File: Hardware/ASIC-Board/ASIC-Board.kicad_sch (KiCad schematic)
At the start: 30 parts, among them J201 Conn_02x20_Odd_Even, J202 Keyboard, J203 Edge_Connector, U201 MegaDuck_Interface_CPU, U202 74LS241, U203 by ManCloud, Y201 Crystal

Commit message: fixed orientation of EXT-Header
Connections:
- net CP: now also J201.30 (Pin_30); no longer J201.12 (Pin_12)
- net CPG: now also J201.31 (Pin_31); no longer J201.9 (Pin_9)
- net CPL: now also J201.27 (Pin_27); no longer J201.13 (Pin_13)
- net EDGE_14: now also J201.25 (Pin_25); no longer J201.15 (Pin_15)
- net FR: now also J201.34 (Pin_34); no longer J201.8 (Pin_8)
- net GND: now also J201.26 (Pin_26); no longer J201.16 (Pin_16)
- net LD0: now also J201.32 (Pin_32); no longer J201.10 (Pin_10)
- net LD1: now also J201.33 (Pin_33); no longer J201.7 (Pin_7)
- net P14_EXT: now also J201.35 (Pin_35); no longer J201.5 (Pin_5)
- net S: now also J201.28 (Pin_28); no longer J201.14 (Pin_14)
- net SCK_EXT: now also J201.36 (Pin_36); no longer J201.6 (Pin_6)
- net SIN_EXT: now also J201.37 (Pin_37); no longer J201.3 (Pin_3)
- net SOUT_EXT: now also J201.38 (Pin_38); no longer J201.4 (Pin_4)
- net ST: now also J201.29 (Pin_29); no longer J201.11 (Pin_11)
- net VCC: now also J201.39 (Pin_39), J201.40 (Pin_40); no longer J201.1 (Pin_1), J201.2 (Pin_2)
- net at R206.2, U202.2 (I0a): now also J201.20 (Pin_20); no longer J201.22 (Pin_22)
- net at R203.2, U202.11 (I0b): now also J201.22 (Pin_22); no longer J201.20 (Pin_20)
- net at R201.2, U202.13 (I1b): now also J201.21 (Pin_21); no longer J201.19 (Pin_19)
- net at R205.2, U202.4 (I1a): now also J201.15 (Pin_15); no longer J201.25 (Pin_25)
- net at J201.17 (Pin_17): now also U201.68; no longer U201.70
- net at J201.18 (Pin_18): now also U201.69; no longer U201.71
- net at U201.6: now also J201.19 (Pin_19); no longer J201.21 (Pin_21)
- net at J201.23 (Pin_23): now also U201.70; no longer U201.68
- net at J201.24 (Pin_24): now also U201.71; no longer U201.69
- net at U202.17 (I3b): now also J201.16 (Pin_16); no longer J201.26 (Pin_26)
- net at U201.65: now also J201.13 (Pin_13); no longer J201.27 (Pin_27)
- net at U202.15 (I2b): now also J201.14 (Pin_14); no longer J201.28 (Pin_28)
- net at U201.42: now also J201.11 (Pin_11); no longer J201.29 (Pin_29)
- net at U201.59: now also J201.12 (Pin_12); no longer J201.30 (Pin_30)
- net at U201.39: now also J201.9 (Pin_9); no longer J201.31 (Pin_31)
- net at U201.58: now also J201.10 (Pin_10); no longer J201.32 (Pin_32)
- net at U201.12: now also J201.7 (Pin_7); no longer J201.33 (Pin_33)
- net at U201.11: now also J201.8 (Pin_8); no longer J201.34 (Pin_34)
- net at U201.14: now also J201.5 (Pin_5); no longer J201.35 (Pin_35)
- net at U201.13: now also J201.6 (Pin_6); no longer J201.36 (Pin_36)
- net at U201.16: now also J201.3 (Pin_3); no longer J201.37 (Pin_37)
- net at U201.15: now also J201.4 (Pin_4); no longer J201.38 (Pin_38)
- net at U201.18: now also J201.1 (Pin_1); no longer J201.39 (Pin_39)
- net at U201.17: now also J201.2 (Pin_2); no longer J201.40 (Pin_40)
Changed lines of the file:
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@@
 	(symbol
 		(lib_id "Connector_Generic:Conn_02x20_Odd_Even")
-		(at 90.17 233.68 0)
+		(at 90.17 236.22 0)
+		(mirror x)
 		(unit 1)
 		(exclude_from_sim no)
@@
 		(dnp no)
 		(property "Reference" "J201"
-			(at 91.44 204.47 0)
+			(at 91.44 265.43 0)
 			(effects
 				(font
@@
 		)
 		(property "Value" "Conn_02x20_Odd_Even"
-			(at 91.44 207.01 0)
+			(at 91.44 262.89 0)
 			(effects
 				(font
@@
 		)
 		(property "Footprint" "Connector_PinHeader_2.54mm:PinHeader_2x20_P2.54mm_Vertical"
-			(at 90.17 233.68 0)
+			(at 90.17 236.22 0)
 			(effects
 				(font
@@
 		)
 		(property "Datasheet" "~"
-			(at 90.17 233.68 0)
+			(at 90.17 236.22 0)
 			(effects
 				(font
@@
 		)
 		(property "Description" "Generic connector, double row, 02x20, odd/even pin numbering scheme (row 1 odd numbers, row 2 even numbers), script generated (kicad-library-utils/schlib/autogen/connector/)"
-			(at 90.17 233.68 0)
+			(at 90.17 236.22 0)
 			(effects
 				(font

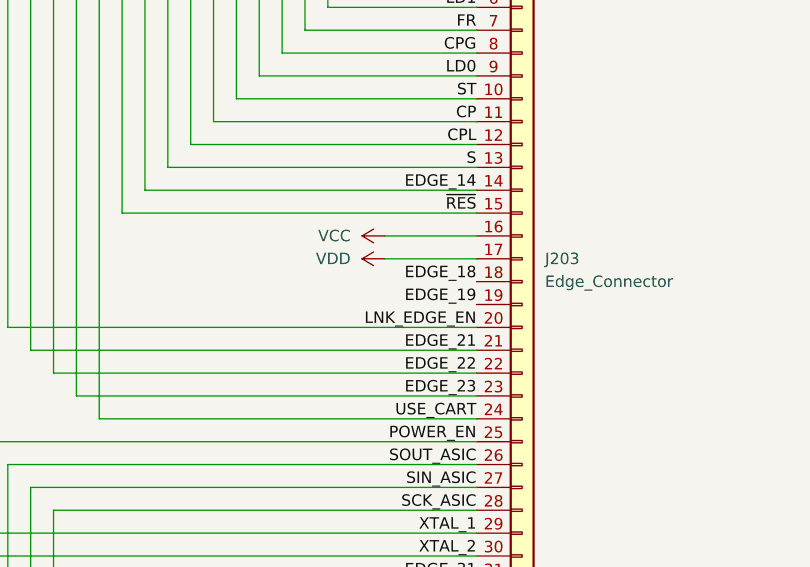
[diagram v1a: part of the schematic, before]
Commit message: Fixed error in Audio-Mixer - Added more signal names
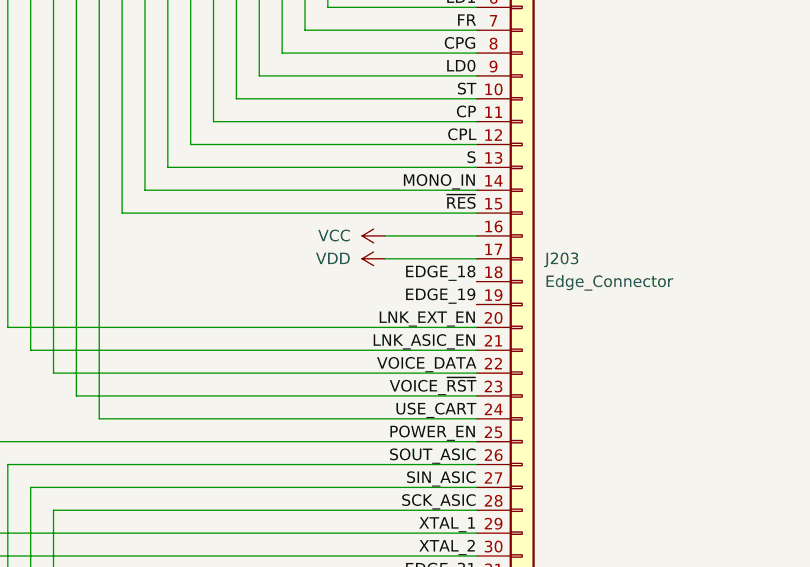
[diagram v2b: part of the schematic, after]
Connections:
- net EDGE_14 renamed MONO_IN
- net EDGE_21 renamed LNK_ASIC_EN
- net EDGE_22 renamed VOICE_DATA
- net EDGE_23 renamed VOICE_~{RST}
- net LNK_EDGE_EN renamed LNK_EXT_EN
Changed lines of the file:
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@@
+		)
+	)
+	(label "VOICE_~{RST}"
+		(at 353.06 213.36 180)
+		(effects
+			(font
+				(size 1.27 1.27)
+			)
+			(justify right bottom)
 		)
 	)
@@
 		)
 	)
-	(label "EDGE_23"
-		(at 353.06 213.36 180)
-		(effects
-			(font
-				(size 1.27 1.27)
-			)
-			(justify right bottom)
-		)
-	)
 	(label "SCK_ASIC"
 		(at 353.06 226.06 180)
@@
 		)
 	)
-	(label "EDGE_21"
+	(label "LNK_ASIC_EN"
 		(at 353.06 208.28 180)
 		(effects
@@
 		)
 	)
-	(label "EDGE_14"
+	(label "MONO_IN"
 		(at 353.06 190.5 180)
 		(effects
@@
 		)
 	)
-	(label "EDGE_22"
-		(at 353.06 210.82 180)
-		(effects
-			(font
-				(size 1.27 1.27)
-			)
-			(justify right bottom)
-		)
-	)
 	(label "XTAL_1"
 		(at 353.06 228.6 180)
@@
 		)
 	)
-	(label "LNK_EDGE_EN"
+	(label "LNK_EXT_EN"
 		(at 353.06 205.74 180)
 		(effects
@@
 		(effects
 			(font
+				(size 1.27 1.27)
+			)
+			(justify right bottom)
+		)
+	)
+	(label "VOICE_DATA"
+		(at 353.06 210.82 180)
+		(effects
+			(font
